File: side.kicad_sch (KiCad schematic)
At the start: 85 parts, among them J1 Conn_01x02, J2 SWD_Connector, J3 USB_C_Receptacle_USB2.0_16P, SW1 Reset Button, SW10 SW_Push, SW11 SW_Push, SW12 SW_Push, SW13 SW_Push, SW14 SW_Push, SW15 SW_Push, SW16 SW_Push, SW17 SW_Push, SW18 SW_Push, SW19 SW_Push, SW20 SW_Push, SW21 SW_Push, SW22 SW_Push, SW23 SW_Push, SW3 SW_Push, SW4 SW_Push, SW5 SW_Push, SW6 SW_Push, SW7 SW_Push, SW8 SW_Push, SW9 SW_Push, U2 USBLC6-2SC6, U7 nRF52833_QDxx, Y1 32MHz, Y3 32.768 kHz

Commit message: cleand up things
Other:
- note added: "Test Points"
- moved on the sheet: AE65, C10, C11, C12, C13, C14, C19, C39, C4, C41, C43, C5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

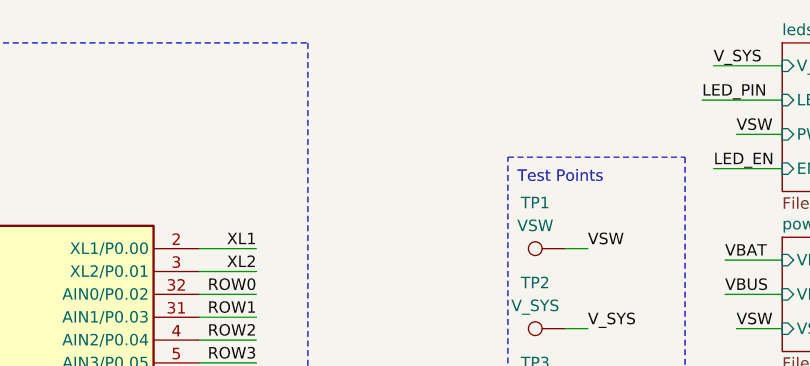
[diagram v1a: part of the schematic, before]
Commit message: added logo, cleaned up traces
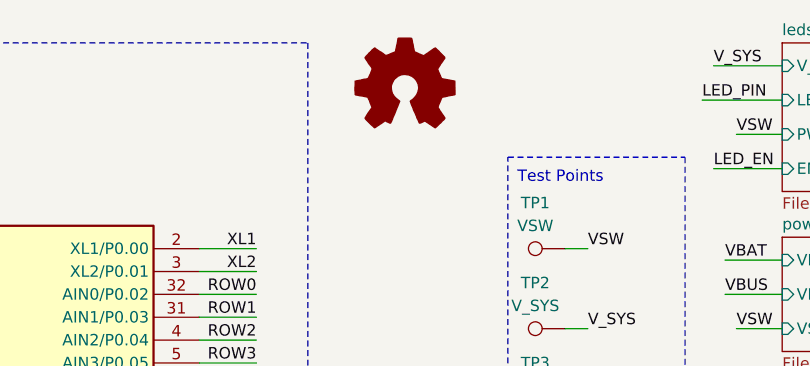
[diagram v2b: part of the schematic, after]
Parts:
- added LOGO2: Logo_Open_Hardware_Small, koeg-logo:BM logo, symbol Graphic:Logo_Open_Hardware_Small
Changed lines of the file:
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@@
+	)
+	(symbol
+		(lib_id "Graphic:Logo_Open_Hardware_Small")
+		(at 113.03 20.32 0)
+		(unit 1)
+		(exclude_from_sim no)
+		(in_bom no)
+		(on_board yes)
+		(dnp no)
+		(fields_autoplaced yes)
+		(property "Reference" "LOGO2"
+			(at 113.03 13.335 0)
+			(effects
+				(font
+					(size 1.27 1.27)
+				)
+				(hide yes)
+			)
+		)
+		(property "Value" "Logo_Open_Hardware_Small"
+			(at 113.03 26.035 0)
+			(effects
+				(font
+					(size 1.27 1.27)
+				)
+				(hide yes)
+			)
+		)
+		(property "Footprint" "koeg-logo:BM logo"
+			(at 113.03 20.32 0)
+			(effects
+				(font
+					(size 1.27 1.27)
+				)
+				(hide yes)
+			)
+		)
+		(property "Datasheet" "~"
+			(at 113.03 20.32 0)
+			(effects
+				(font
+					(size 1.27 1.27)
+				)
+				(hide yes)
+			)
+		)
+		(property "Description" "Open Hardware logo, small"
+			(at 113.03 20.32 0)
+			(effects
+				(font
+					(size 1.27 1.27)
+				)
+				(hide yes)
+			)
+		)
+		(property "Sim.Enable" "0"
+			(at 113.03 20.32 0)
+			(effects
+				(font
+					(size 1.27 1.27)
+				)
+				(hide yes)
+			)
+		)
+		(instances
+			(project ""
+				(path "/2b736a6b-c6e2-42fa-94c9-e384d663659b/4bb325fd-7371-4bed-a032-a434391e94c9"
+					(reference "LOGO1")
+					(unit 1)
+				)
+				(path "/2b736a6b-c6e2-42fa-94c9-e384d663659b/8d53595d-91b9-4d70-adec-5245477c92d0"
+					(reference "LOGO2")
+					(unit 1)
+				)
+			)
+		)
 	)
 	(symbol

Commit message: checked schematic again, fixed bugs
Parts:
- renumbered LOGO2 to LOGO1
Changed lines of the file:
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@@
 		(dnp no)
 		(fields_autoplaced yes)
-		(property "Reference" "LOGO2"
+		(property "Reference" "LOGO1"
 			(at 113.03 13.335 0)
 			(effects
@@
 			(at 113.03 20.32 0)
 			(effects
-				(font
-					(size 1.27 1.27)
-				)
-				(hide yes)
-			)
-		)
-		(property "Sim.Enable" "0"
-			(at 113.03 20.32 0)
-			(effects

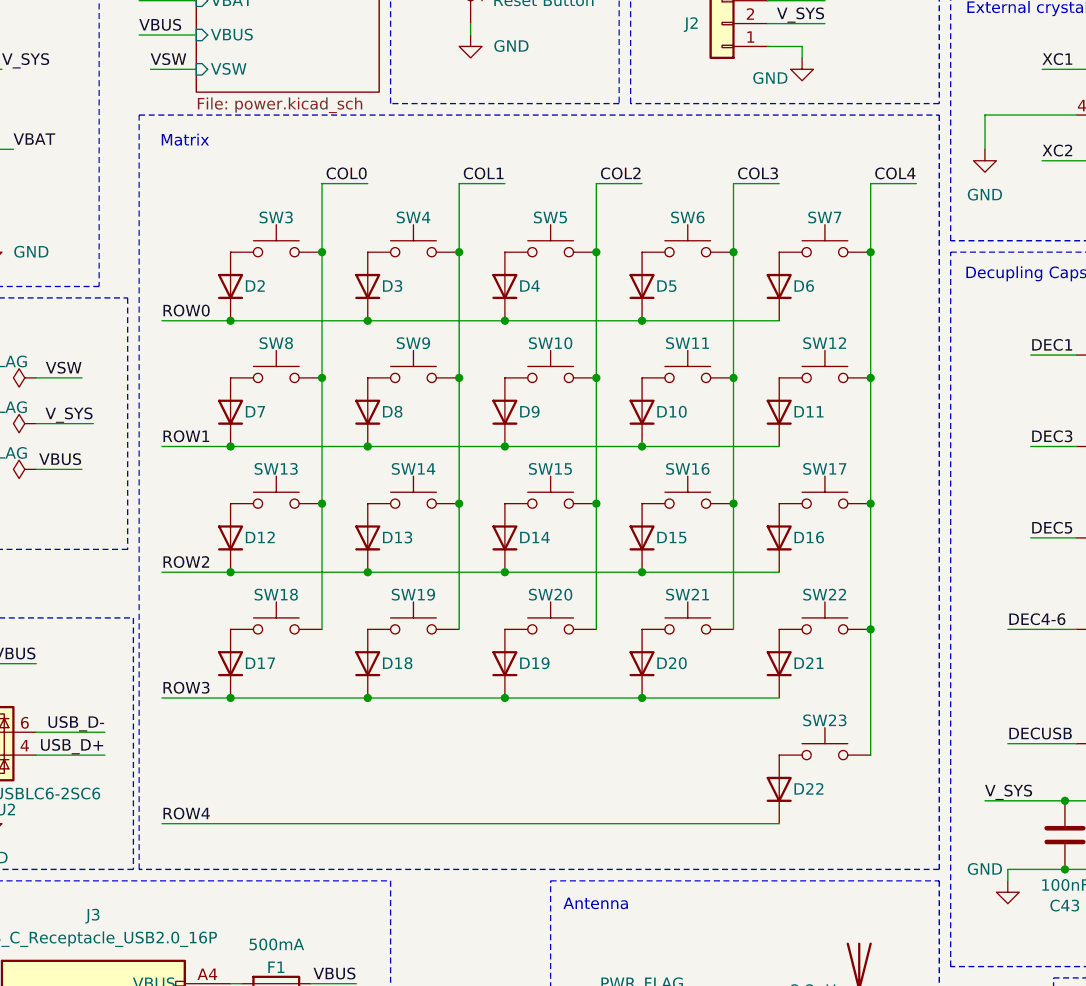
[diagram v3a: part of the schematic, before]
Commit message: fixed edge cuts, switched to marbastlib switches
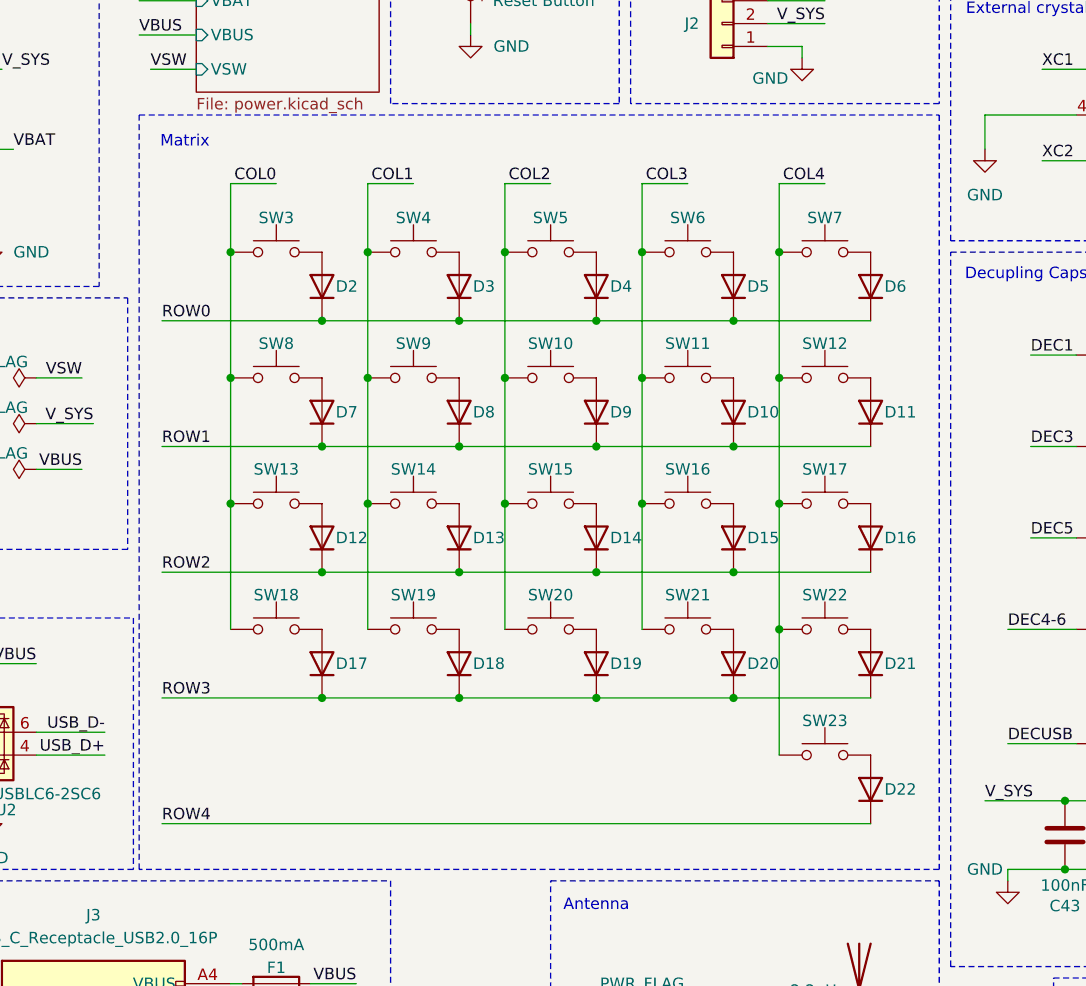
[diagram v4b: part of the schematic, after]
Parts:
- SW10, SW11, SW12, SW13, SW14, SW15, SW16, SW17, SW18, SW19, SW20, SW21, SW22, SW3, SW4, SW5, SW6, SW7, SW8, SW9: footprint PCM_Switch_Keyboard_Hotswap_Kailh:SW_Hotswap_Kailh_Choc_V1V2_1.00u -> PCM_marbastlib-choc:SW_choc_v1_HS_CPG135001S30_1u
- SW23: footprint PCM_Switch_Keyboard_Hotswap_Kailh:SW_Hotswap_Kailh_Choc_V1V2_1.75u_90deg -> PCM_marbastlib-choc:SW_choc_v1_HS_CPG135001S30_1u
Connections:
- net COL0: now also SW13.1, SW18.1, SW3.1, SW8.1; no longer SW13.2, SW18.2, SW3.2, SW8.2
- net COL1: now also SW14.1, SW19.1, SW4.1, SW9.1; no longer SW14.2, SW19.2, SW4.2, SW9.2
- net COL2: now also SW10.1, SW15.1, SW20.1, SW5.1; no longer SW10.2, SW15.2, SW20.2, SW5.2
- net COL3: now also SW11.1, SW16.1, SW21.1, SW6.1; no longer SW11.2, SW16.2, SW21.2, SW6.2
- net COL4: now also SW12.1, SW17.1, SW22.1, SW23.1, SW7.1; no longer SW12.2, SW17.2, SW22.2, SW23.2, SW7.2
- net at D14.2 (A): now also SW15.2; no longer SW15.1
- net at D2.2 (A): now also SW3.2; no longer SW3.1
- net at D22.2 (A): now also SW23.2; no longer SW23.1
- net at D11.2 (A): now also SW12.2; no longer SW12.1
- net at D15.2 (A): now also SW16.2; no longer SW16.1
- net at D20.2 (A): now also SW21.2; no longer SW21.1
- net at D3.2 (A): now also SW4.2; no longer SW4.1
- net at D7.2 (A): now also SW8.2; no longer SW8.1
- net at D12.2 (A): now also SW13.2; no longer SW13.1
- net at D10.2 (A): now also SW11.2; no longer SW11.1
- net at D17.2 (A): now also SW18.2; no longer SW18.1
- net at D13.2 (A): now also SW14.2; no longer SW14.1
- net at D19.2 (A): now also SW20.2; no longer SW20.1
- net at D4.2 (A): now also SW5.2; no longer SW5.1
- net at D8.2 (A): now also SW9.2; no longer SW9.1
- net at D16.2 (A): now also SW17.2; no longer SW17.1
- net at D18.2 (A): now also SW19.2; no longer SW19.1
- net at D21.2 (A): now also SW22.2; no longer SW22.1
- net at D5.2 (A): now also SW6.2; no longer SW6.1
- net at D6.2 (A): now also SW7.2; no longer SW7.1
- net at D9.2 (A): now also SW10.2; no longer SW10.1
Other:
- moved on the sheet: D10, D11, D12, D13, D14, D15, D16, D17, D18, D19, D2, D20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

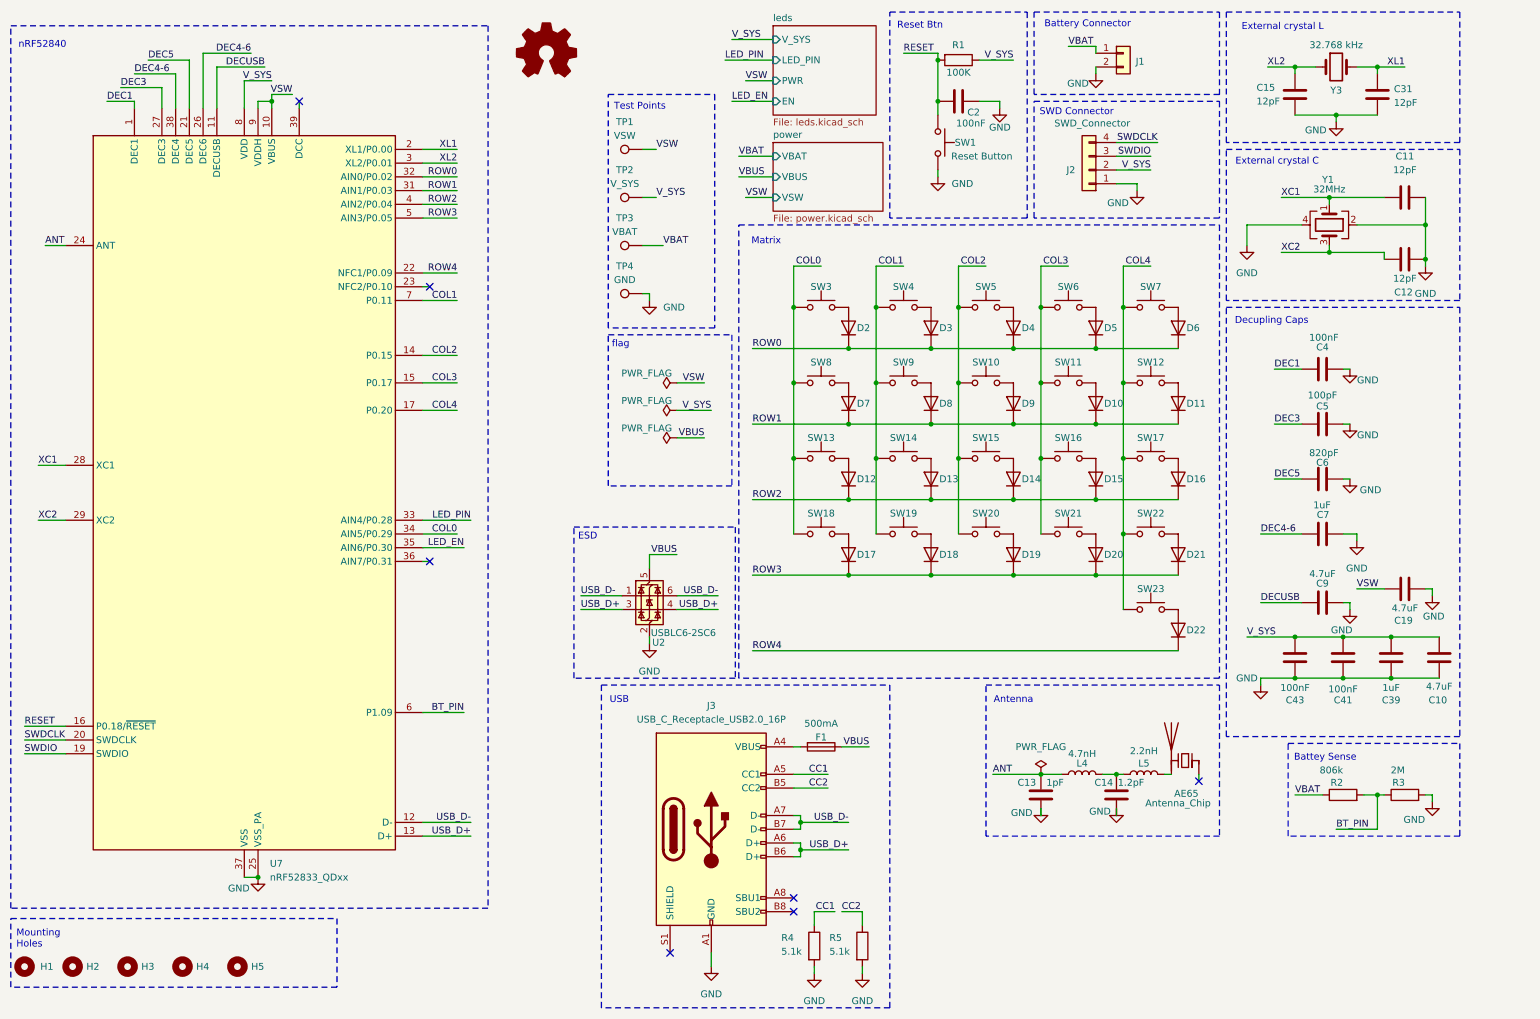
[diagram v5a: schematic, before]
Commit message: made progress, added xiao libray, removed almost all of the old schmeatic, started ot edit pcb
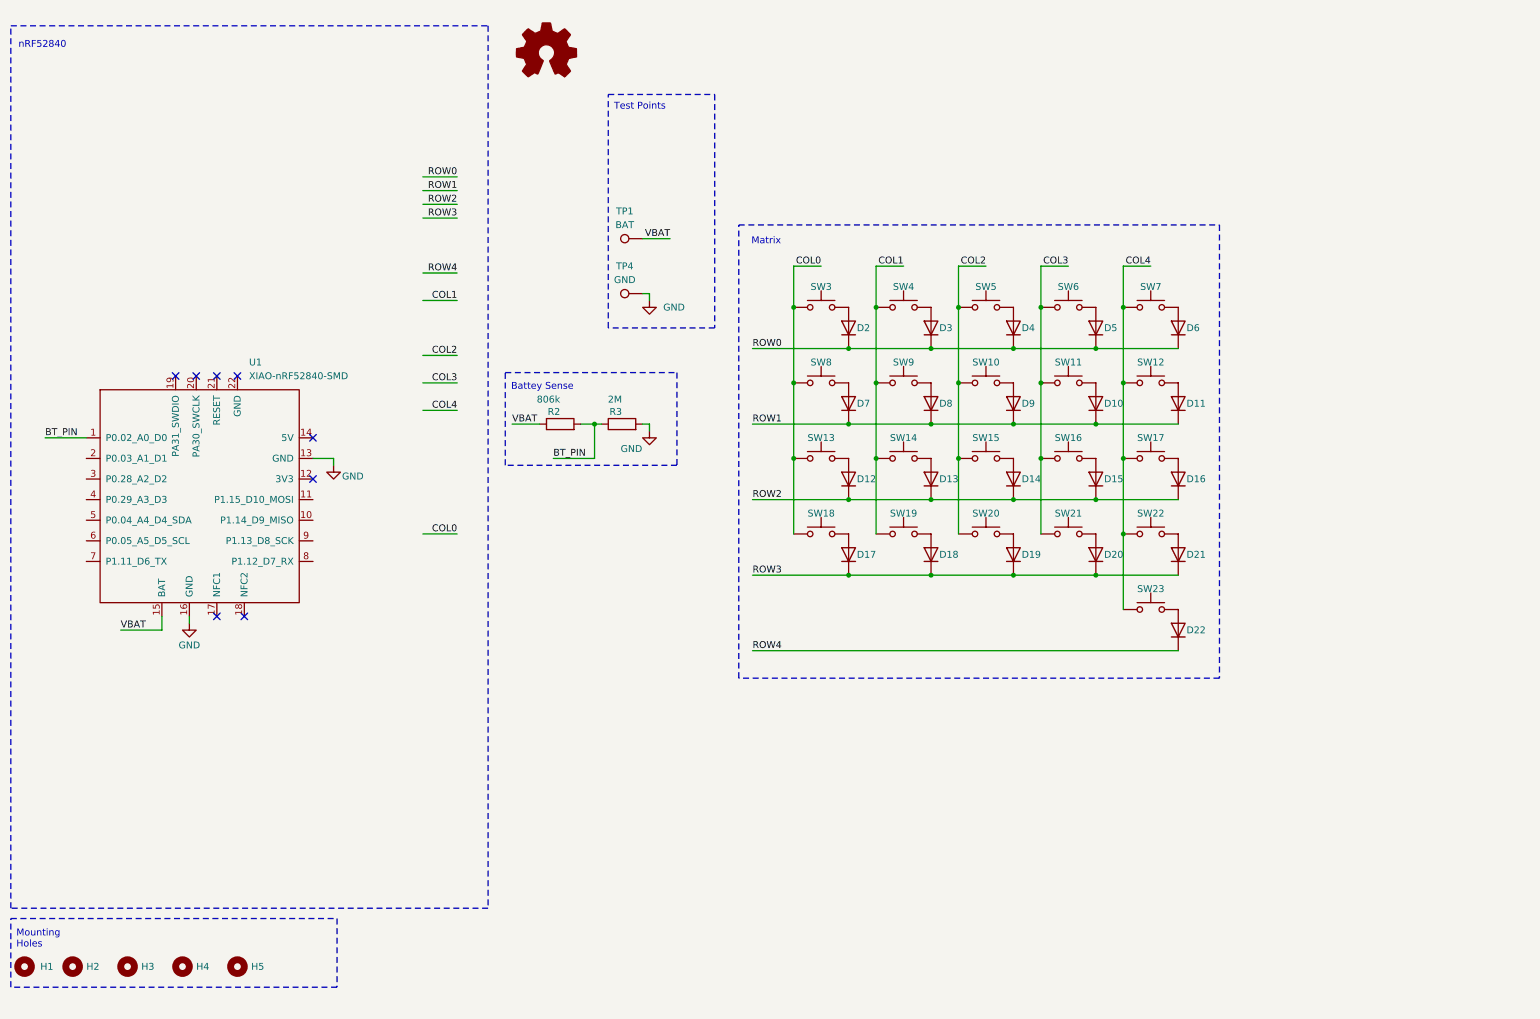
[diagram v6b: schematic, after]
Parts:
- removed AE65: Antenna_Chip, 2450AT42A100E:ANTC5020X110N, symbol Device:Antenna_Chip
- removed C10, C19: 4.7uF, Capacitor_SMD:C_0603_1608Metric, symbol Device:C
- removed C11, C12, C15, C31: 12pF, Capacitor_SMD:C_0402_1005Metric, symbol Device:C
- removed C13: 1pF, Capacitor_SMD:C_0402_1005Metric, symbol Device:C
- removed C14: 1.2pF, Capacitor_SMD:C_0402_1005Metric, symbol Device:C
- removed C2, C4, C41, C43: 100nF, Capacitor_SMD:C_0402_1005Metric, symbol Device:C
- removed C39, C7: 1uF, Capacitor_SMD:C_0402_1005Metric, symbol Device:C
- removed C5: 100pF, Capacitor_SMD:C_0402_1005Metric, symbol Device:C
- removed C6: 820pF, Capacitor_SMD:C_0402_1005Metric, symbol Device:C
- removed C9: 4.7uF, Capacitor_SMD:C_0402_1005Metric, symbol Device:C
- removed F1: 500mA, Fuse:Fuse_0603_1608Metric, symbol Device:Fuse
- removed J1: Conn_01x02, Connector_PinHeader_1.00mm:PinHeader_1x02_P1.00mm_Vertical, symbol Connector_Generic:Conn_01x02
- removed J2: SWD_Connector, Connector_PinHeader_1.00mm:PinHeader_1x04_P1.00mm_Vertical, symbol Connector_Generic:Conn_01x04
- removed J3: USB_C_Receptacle_USB2.0_16P, Connector_USB:USB_C_Receptacle_G-Switch_GT-USB-7010ASV, symbol Connector:USB_C_Receptacle_USB2.0_16P
- removed L4: 4.7nH, Inductor_SMD:L_0402_1005Metric, symbol Device:L
- removed L5: 2.2nH, Inductor_SMD:L_0402_1005Metric, symbol Device:L
- removed R1: 100K, Resistor_SMD:R_0402_1005Metric, symbol Device:R
- removed R4, R5: 5.1k, Resistor_SMD:R_0402_1005Metric, symbol Device:R
- removed SW1: Reset Button, Button_Switch_SMD:SW_SPST_TL3342, symbol Switch:SW_Push
- removed TP2: V_SYS, TestPoint:TestPoint_Pad_D2.0mm, symbol Connector:TestPoint
- removed TP3: VBAT, TestPoint:TestPoint_Pad_D2.0mm, symbol Connector:TestPoint
- removed U2: USBLC6-2SC6, Package_TO_SOT_SMD:SOT-23-6, symbol Power_Protection:USBLC6-2SC6
- removed U7: nRF52833_QDxx, Package_DFN_QFN:QFN-40-1EP_5x5mm_P0.4mm_EP3.6x3.6mm, symbol MCU_Nordic:nRF52833_QDxx
- removed Y1: 32MHz, Crystal:Crystal_SMD_2520-4Pin_2.5x2.0mm, symbol Device:Crystal_GND24
- removed Y3: 32.768 kHz, Crystal:Crystal_SMD_3215-2Pin_3.2x1.5mm, symbol Device:Crystal
- added U1: XIAO-nRF52840-SMD, Seeed Studio XIAO Series Library:XIAO-nRF52840-SMD, symbol Seeed_Studio_XIAO_Series:XIAO-nRF52840-SMD
- R2, R3: footprint Resistor_SMD:R_0402_1005Metric -> Resistor_SMD:R_0805_2012Metric
- TP1: value VSW -> BAT
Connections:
- net VSW is gone; now on net VBAT: TP1.1
- net BT_PIN: now also U1.1 (P0.02_A0_D0)
- net GND: now also U1.13 (GND), U1.16 (GND)
- net VBAT: now also U1.15 (BAT)
- no-connect marks 7 -> 8
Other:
- removed sheet leds
- removed sheet power
- note removed: "Antenna"
- note removed: "Battery Connector"
- note removed: "Decupling Caps"
- note removed: "ESD"
- note removed: "External crystal C"
- note removed: "External crystal L"
- note removed: "Reset Btn"
- note removed: "SWD Connector"
- note removed: "USB"
- note removed: "flag"
- moved on the sheet: R2, R3
